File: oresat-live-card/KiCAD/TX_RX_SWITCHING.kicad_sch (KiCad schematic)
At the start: 38 parts, among them J11 2X1_TH_JUMPER, J15 2X1_TH_JUMPER, U23 SN74LVC1G32QDBVRQ1, U24 LTC6994-1, U25 LTC6994-1, U26 SN74LV1T34, U32 SN74LV1T34, U34 QPC1022, U35 SN74LVC1G32QDBVRQ1, U36 QPC1022

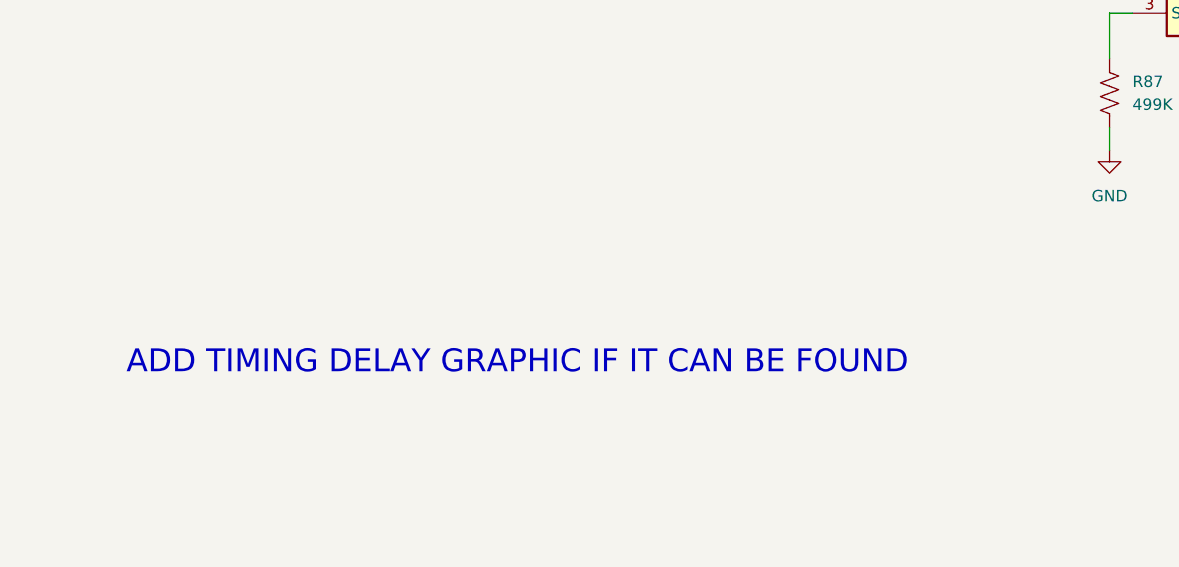
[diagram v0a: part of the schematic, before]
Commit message: Removed or-gate U6 and jumper J5, added Tx/Rx timing delay graphic to schematic, updated all symbols from oresat library, added new components to PCB and started grouping them
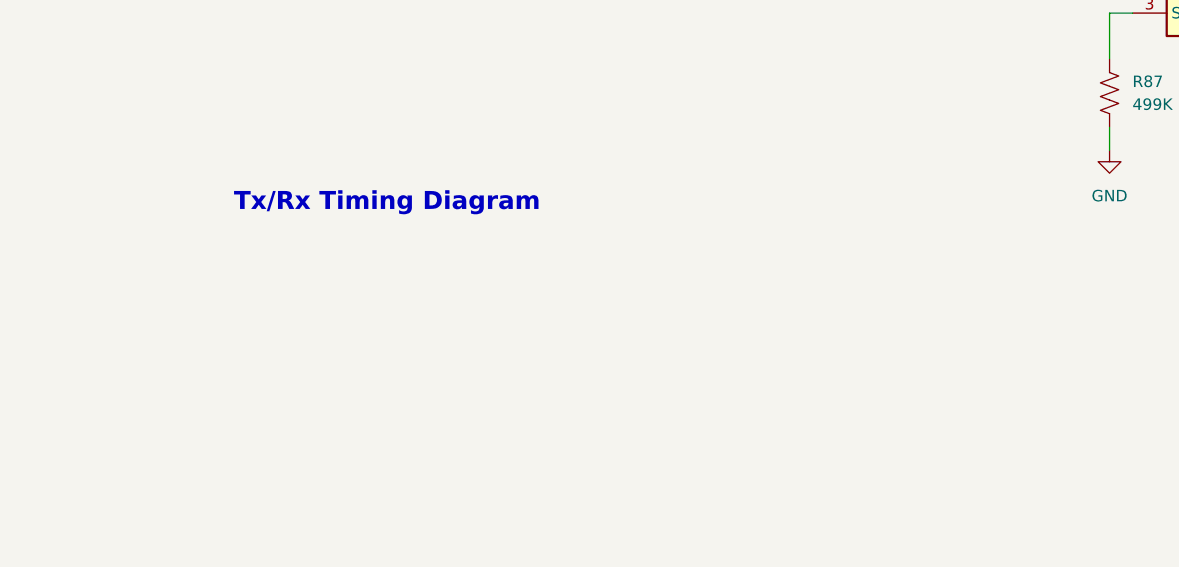
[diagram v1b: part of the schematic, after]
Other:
- note added: "Tx/Rx Timing Diagram"
- note removed: "ADD TIMING DELAY GRAPHIC IF IT CAN BE FOUND"

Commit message: Changed C118, R124, R125 from 0603 to 0402, starting layout and routing
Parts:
- C116: footprint Resistor_SMD:R_0402_1005Metric -> Capacitor_SMD:C_0402_1005Metric
- C118: footprint Resistor_SMD:R_0603_1608Metric -> Capacitor_SMD:C_0402_1005Metric
- R124, R125: footprint Resistor_SMD:R_0603_1608Metric -> Resistor_SMD:R_0402_1005Metric
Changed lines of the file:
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@@
 			)
 		)
-		(property "Footprint" "Resistor_SMD:R_0603_1608Metric"
+		(property "Footprint" "Resistor_SMD:R_0402_1005Metric"
 			(at 296.164 198.374 90)
 			(effects
@@
 			)
 		)
-		(property "Footprint" "Resistor_SMD:R_0603_1608Metric"
+		(property "Footprint" "Capacitor_SMD:C_0402_1005Metric"
 			(at 340.36 190.5 0)
 			(effects
@@
 			)
 		)
-		(property "Footprint" "Resistor_SMD:R_0603_1608Metric"
+		(property "Footprint" "Resistor_SMD:R_0402_1005Metric"
 			(at 308.864 198.374 90)
 			(effects
@@
 			)
 		)
-		(property "Footprint" "Resistor_SMD:R_0402_1005Metric"
+		(property "Footprint" "Capacitor_SMD:C_0402_1005Metric"
 			(at 328.93 190.5 0)
 			(effects

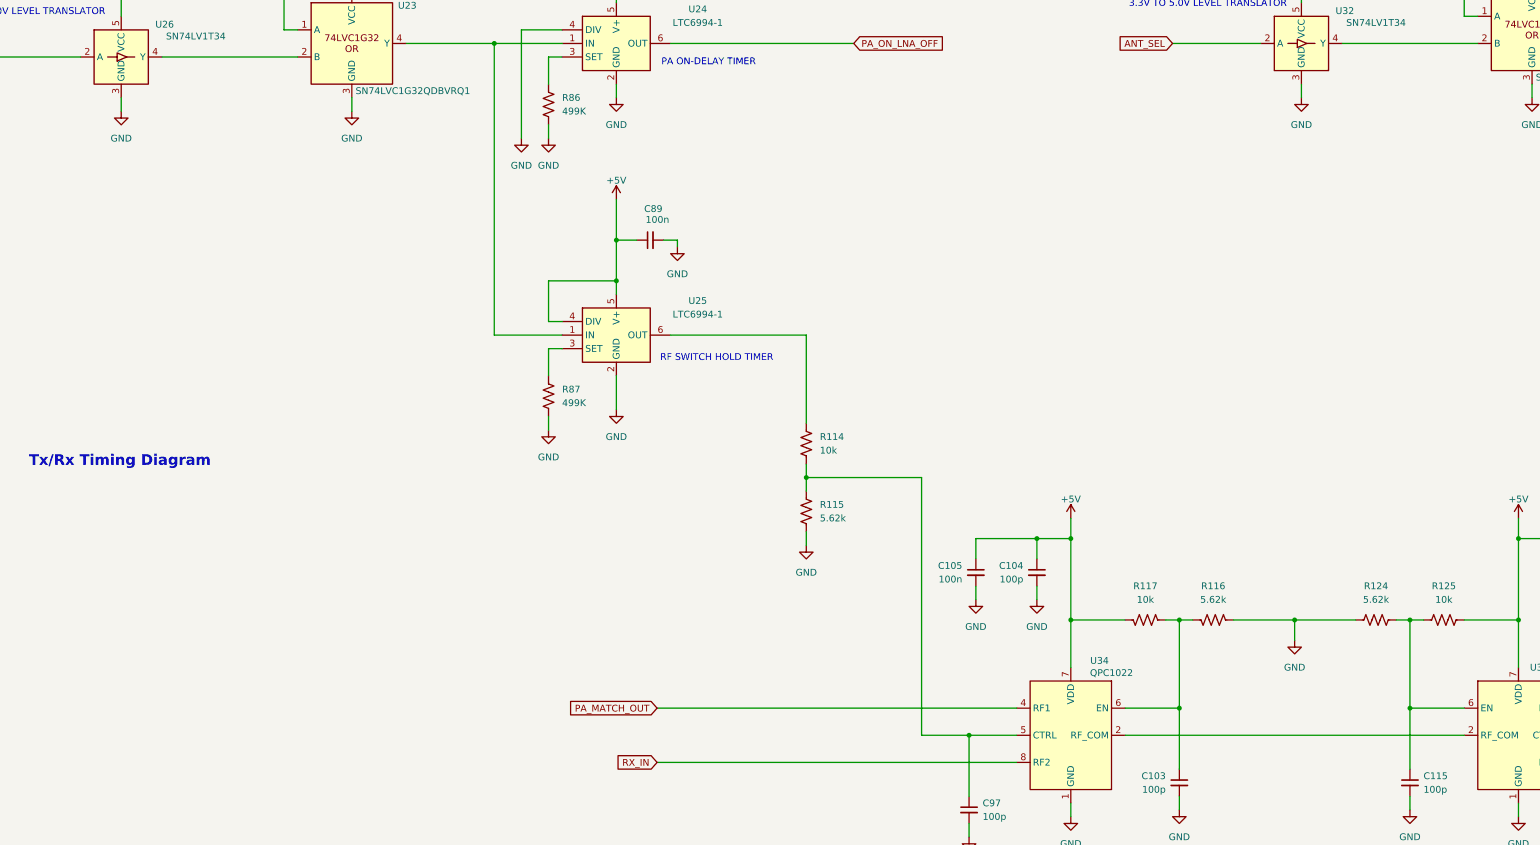
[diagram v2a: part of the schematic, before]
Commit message: added notes to schematic, added footprints to Fl1 & U29 & U23,35, updated changes to board
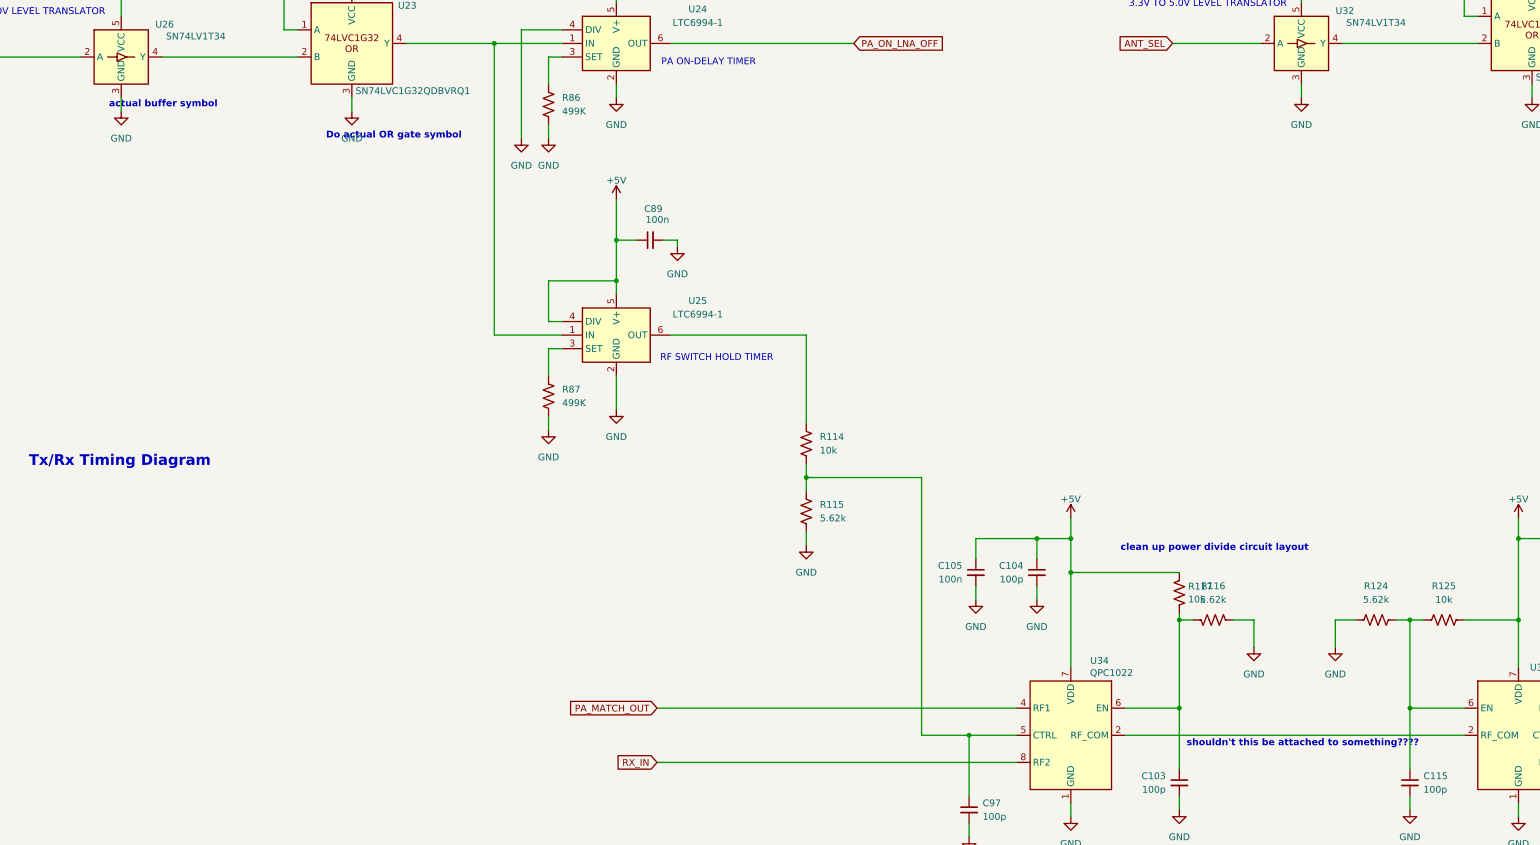
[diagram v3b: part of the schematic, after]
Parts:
- U23, U35: footprint (none) -> Package_TO_SOT_SMD:SOT-23-5
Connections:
- net +5V: now also R117.1; no longer R117.2
- net at C103.1, R116.2, U34.6 (EN): now also R117.2; no longer R117.1
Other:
- note added: "Do actual OR gate symbol"
- note added: "actual buffer symbol"
- note added: "clean up power divide circuit layout"
- note added: "shouldn't this be attached to something????"
- moved on the sheet: R117

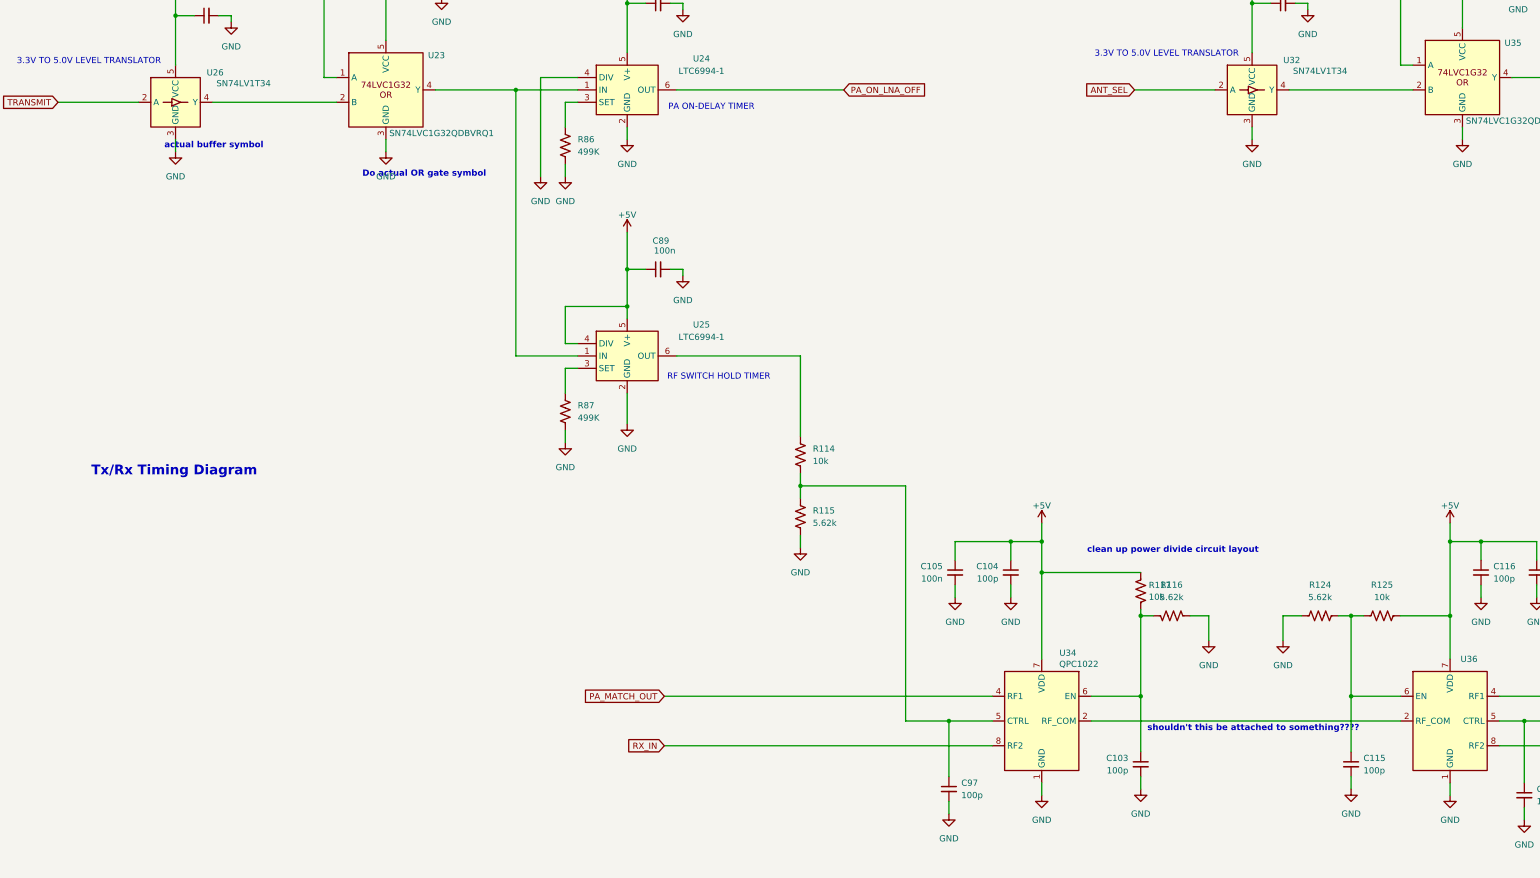
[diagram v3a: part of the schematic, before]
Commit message: swapped placement of R105 and R88, changed R109 from 100 to 56 ohms, relabelled PWR_DET_OUT to RX_DET_OUT, added inverter to TX/RX Control switch and swapped RF1 and RF2
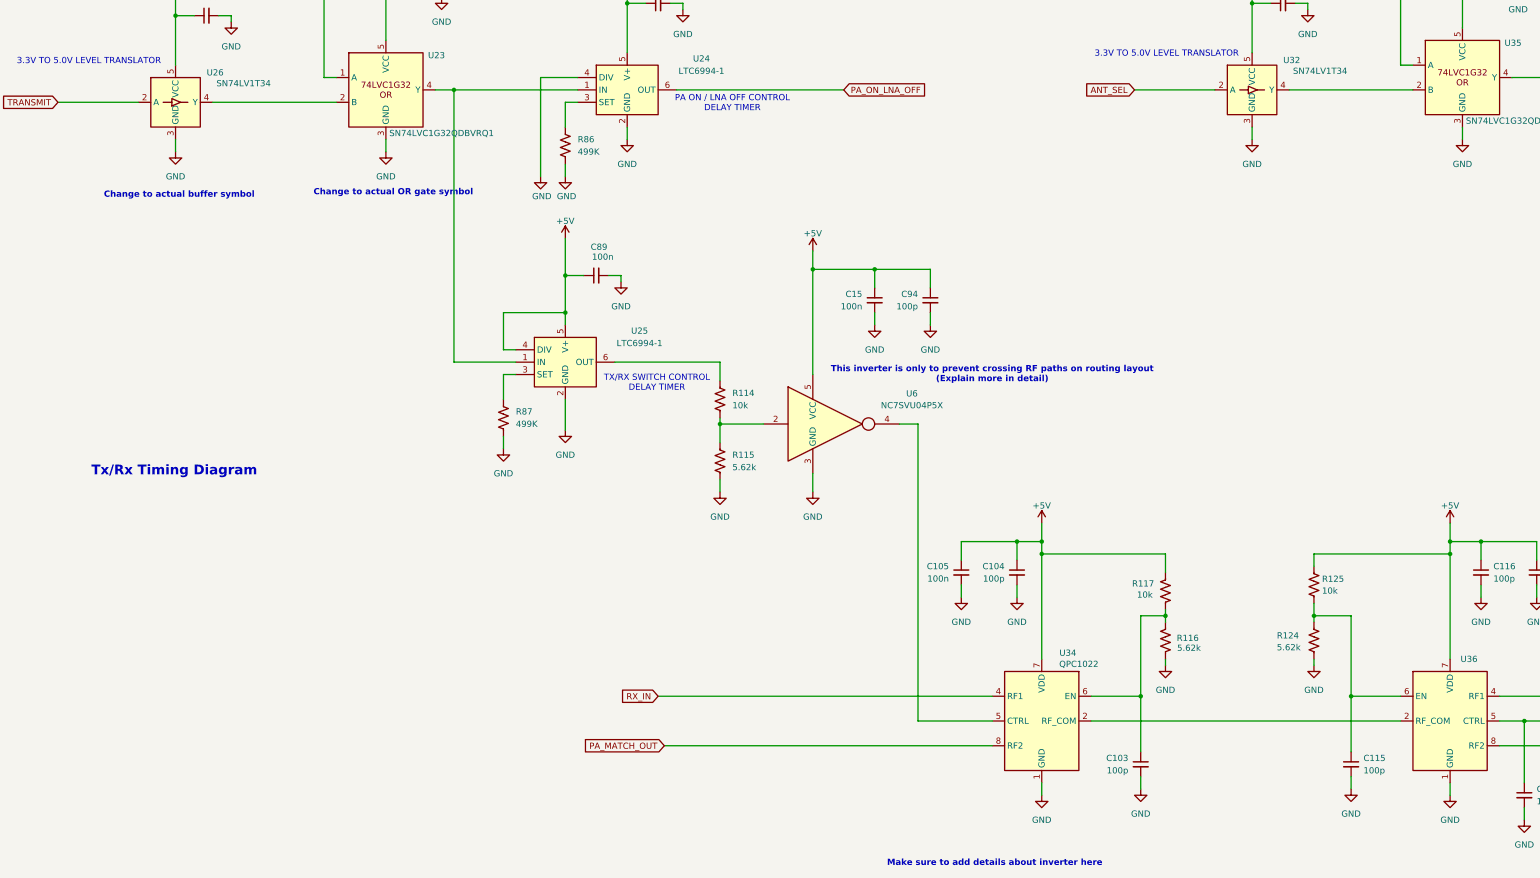
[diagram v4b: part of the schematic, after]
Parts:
- removed C97: 100p, Resistor_SMD:R_0402_1005Metric, symbol Device:C_Small
- added C15: 100n, Resistor_SMD:R_0603_1608Metric, symbol Device:C_Small
- added C94: 100p, Resistor_SMD:R_0402_1005Metric, symbol Device:C_Small
- added U6: NC7SVU04P5X, Package_TO_SOT_SMD:SC-74A-5_1.55x2.9mm_P0.95mm, symbol 74xGxx:NC7SVU04P5X
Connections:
- net +5V: now also C15.1, C94.1, U6.5 (VCC)
- net GND: now also R116.2, C15.2, C94.2, U6.3 (GND); no longer R116.1
- net PA_MATCH_OUT: now also U34.8 (RF2); no longer U34.4 (RF1)
- net RX_IN: now also U34.4 (RF1); no longer U34.8 (RF2)
- net at C103.1, R117.2, U34.6 (EN): now also R116.1; no longer R116.2
- net at R114.1, R115.1: now also U6.2; no longer U34.5 (CTRL)
- new net: U34.5 (CTRL), U6.4
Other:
- note added: "Change to actual OR gate symbol"
- note added: "Change to actual buffer symbol"
- note added: "Make sure to add details about inverter here"
- note added: "PA ON / LNA OFF CONTROL DELAY TIMER"
- note added: "TX/RX SWITCH CONTROL DELAY TIMER"
- note added: "This inverter is only to prevent crossing RF paths on routing layout (Explain more in detail)"
- note removed: "Do actual OR gate symbol"
- note removed: "PA ON-DELAY TIMER"
- note removed: "RF SWITCH HOLD TIMER"
- note removed: "actual buffer symbol"
- note removed: "clean up power divide circuit layout"
- note removed: "shouldn't this be attached to something????"
- moved on the sheet: C104, C105, C89, R114, R115, R116, R117, R124, R125, R87, U25
